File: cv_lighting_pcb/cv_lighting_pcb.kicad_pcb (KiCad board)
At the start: 2 copper layers, 81.3 x 73.7 mm, 27 parts, among them Q1 2N3906, U1 Current Driver, U2 Camera Input, U3 VO617A, U4 Barrel Jack

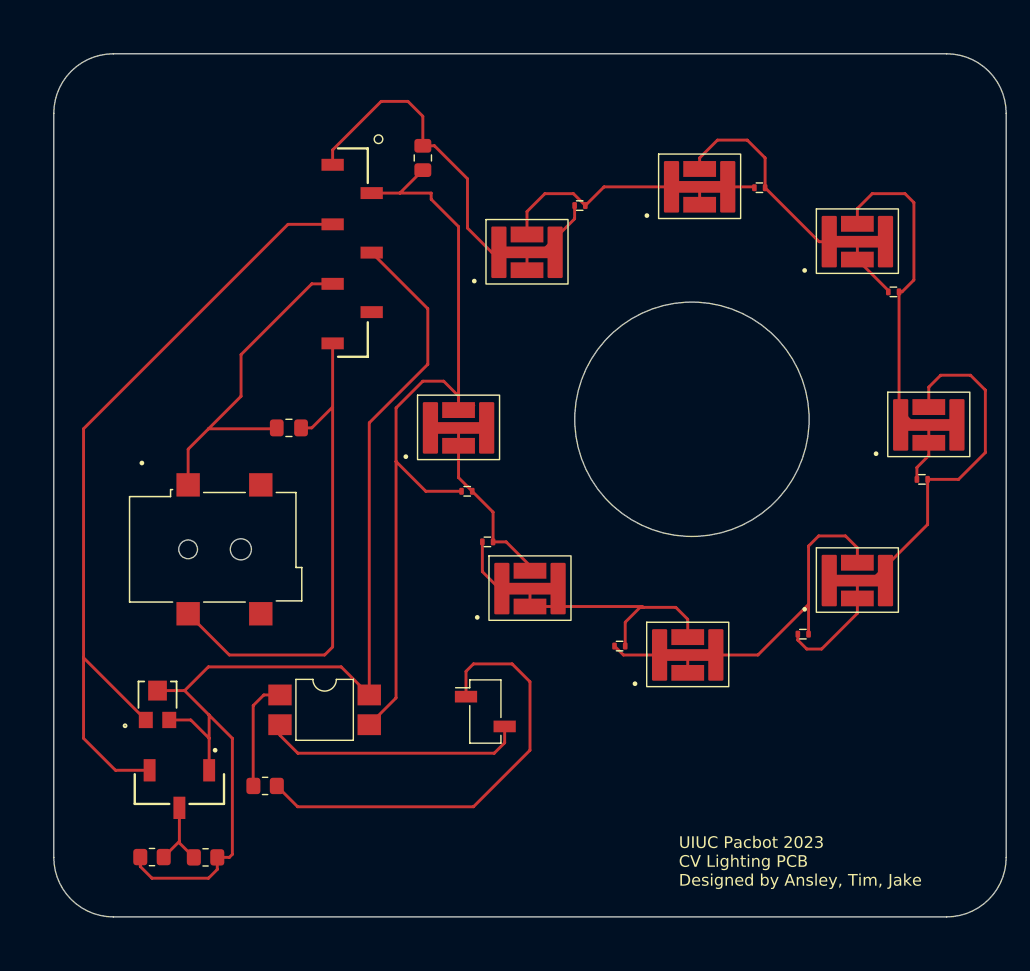
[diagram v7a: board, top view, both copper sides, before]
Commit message: more changes to lighting pcb
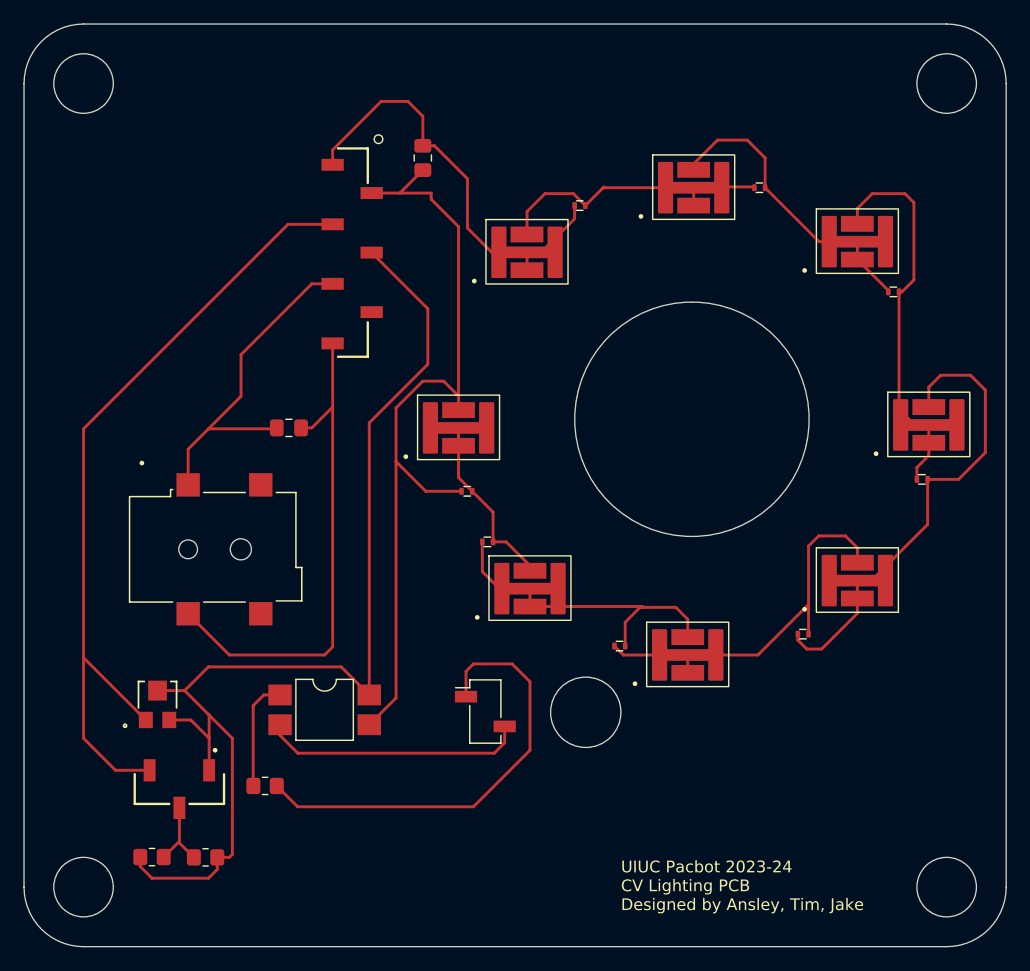
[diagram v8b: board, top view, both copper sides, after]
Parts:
- moved D2 0.51 mm to (156.2, 61.4)
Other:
- board size 81.3 x 73.7 mm -> 83.8 x 78.7 mm
- board text added: "UIUC Pacbot 2023-24 CV Lighting PCB Designed by Ansley, Tim, Jake"
- board text added: "hole for wire from camera to pcb"
- board text removed: "UIUC Pacbot 2023 CV Lighting PCB Designed by Ansley, Tim, Jake"
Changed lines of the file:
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@@
   )
   (footprint "cv_lighting_footprints:LED_SFH4715AS" (layer "F.Cu")
-    (at 156.718 61.359)
+    (at 156.21 61.4322)
     (property "Sheetfile" "cv_lighting_pcb.kicad_sch")
     (property "Sheetname" "")
@@
       (net 12 "Net-(Q1-C)") (pinfunction "C") (pintype "passive") (solder_mask_margin 0.102))
   )
-  (gr_arc (start 106.68 124.46) (mid 103.087898 122.972102) (end 101.6 119.38)
-    (stroke (width 0.1) (type default)) (layer "Edge.Cuts"))
+  (gr_circle (center 177.8 121.92) (end 180.34 121.92)
+    (stroke (width 0.1) (type default)) (fill none) (layer "Edge.Cuts"))
   (gr_circle (center 167.5892 81.9912) (end 167.5892 81.9912)
     (stroke (width 0.1) (type default)) (fill none) (layer "Edge.Cuts"))
-  (gr_line (start 182.88 55.88) (end 182.88 119.38)
+  (gr_line (start 182.88 53.34) (end 182.88 121.92)
     (stroke (width 0.1) (type default)) (layer "Edge.Cuts"))
-  (gr_line (start 106.68 50.8) (end 177.8 50.8)
+  (gr_circle (center 177.8 53.34) (end 180.34 53.34)
+    (stroke (width 0.1) (type default)) (fill none) (layer "Edge.Cuts"))
+  (gr_arc (start 182.88 121.92) (mid 181.392102 125.512102) (end 177.8 127)
     (stroke (width 0.1) (type default)) (layer "Edge.Cuts"))
-  (gr_arc (start 101.6 55.88) (mid 103.087898 52.287898) (end 106.68 50.8)
+  (gr_circle (center 104.14 121.92) (end 106.68 121.92)
+    (stroke (width 0.1) (type default)) (fill none) (layer "Edge.Cuts"))
+  (gr_arc (start 177.8 48.26) (mid 181.392102 49.747898) (end 182.88 53.34)
     (stroke (width 0.1) (type default)) (layer "Edge.Cuts"))
-  (gr_line (start 101.6 119.38) (end 101.6 55.88)
+  (gr_arc (start 104.14 127) (mid 100.547898 125.512102) (end 99.06 121.92)
     (stroke (width 0.1) (type default)) (layer "Edge.Cuts"))
-  (gr_line (start 177.8 124.46) (end 106.68 124.46)
+  (gr_line (start 104.14 48.26) (end 177.8 48.26)
+    (stroke (width 0.1) (type default)) (layer "Edge.Cuts"))
+  (gr_line (start 99.06 121.92) (end 99.06 53.34)
+    (stroke (width 0.1) (type default)) (layer "Edge.Cuts"))
+  (gr_circle (center 104.14 53.34) (end 106.68 53.34)
+    (stroke (width 0.1) (type default)) (fill none) (layer "Edge.Cuts"))
+  (gr_line (start 177.8 127) (end 104.14 127)
     (stroke (width 0.1) (type default)) (layer "Edge.Cuts"))
   (gr_circle (center 156.061042 81.9912) (end 166.061047 81.9912)
     (stroke (width 0.1) (type default)) (fill none) (layer "Edge.Cuts"))
-  (gr_arc (start 182.88 119.38) (mid 181.392102 122.972102) (end 177.8 124.46)
-    (stroke (width 0.1) (type default)) (layer "Edge.Cuts"))
-  (gr_arc (start 177.8 50.8) (mid 181.392102 52.287898) (end 182.88 55.88)
+  (gr_circle (center 147 107) (end 150 107)
+    (stroke (width 0.1) (type default)) (fill none) (layer "Edge.Cuts"))
+  (gr_arc (start 99.06 53.34) (mid 100.547898 49.747898) (end 104.14 48.26)
     (stroke (width 0.1) (type default)) (layer "Edge.Cuts"))
   (gr_circle (center 156.061042 81.9912) (end 176.381042 81.9912)
     (stroke (width 0.1) (type default)) (fill none) (layer "F.Fab"))
-  (gr_text "UIUC Pacbot 2023\nCV Lighting PCB\nDesigned by Ansley, Tim, Jake" (at 154.94 121.92) (layer "F.SilkS")
+  (gr_text "UIUC Pacbot 2023-24\nCV Lighting PCB\nDesigned by Ansley, Tim, Jake" (at 150 124) (layer "F.SilkS")
+    (effects (font (size 1 1) (thickness 0.15)) (justify left bottom))
+  )
+  (gr_text "hole for wire from camera to pcb\n\n" (at 146 113) (layer "F.Fab")
     (effects (font (size 1 1) (thickness 0.15)) (justify left bottom))
   )
@@
     (effects (font (size 1 1) (thickness 0.15)) (justify left bottom))
   )
-  (gr_text "Double check radius of circle based on camera" (at 140.414642 78.6384) (layer "F.Fab")
+  (gr_text "Double check radius of circle based on camera" (at 51 112) (layer "F.Fab")
     (effects (font (size 1 1) (thickness 0.15)) (justify left bottom))
   )
+  (segment (start 148.4862 62.2322) (end 156.21 62.2322) (width 0.25) (layer "F.Cu") (net 1))
   (segment (start 145.9484 62.738) (end 143.51 62.738) (width 0.25) (layer "F.Cu") (net 1))
   (segment (start 161.3206 62.159) (end 161.3916 62.23) (width 0.25) (layer "F.Cu") (net 1))
-  (segment (start 148.5594 62.159) (end 156.718 62.159) (width 0.25) (layer "F.Cu") (net 1))
   (segment (start 141.986 64.262) (end 141.986 66.2188) (width 0.25) (layer "F.Cu") (net 1))
   (segment (start 156.718 62.159) (end 161.3206 62.159) (width 0.25) (layer "F.Cu") (net 1))
   (segment (start 143.51 62.738) (end 141.986 64.262) (width 0.25) (layer "F.Cu") (net 1))
   (segment (start 146.9644 63.754) (end 145.9484 62.738) (width 0.25) (layer "F.Cu") (net 1))
-  (segment (start 156.718 62.159) (end 156.718 63.6808) (width 0.25) (layer "F.Cu") (net 1))
-  (segment (start 146.9644 63.754) (end 148.5594 62.159) (width 0.25) (layer "F.Cu") (net 1))
+  (segment (start 148.4122 62.3062) (end 148.4862 62.2322) (width 0.25) (layer "F.Cu") (net 1))
+  (segment (start 156.21 62.2322) (end 156.21 63.754) (width 0.25) (layer "F.Cu") (net 1))
+  (segment (start 146.9644 63.754) (end 148.4122 62.3062) (width 0.25) (layer "F.Cu") (net 1))
+  (segment (start 148.4122 62.3062) (end 148.5594 62.159) (width 0.25) (layer "F.Cu") (net 1))
   (segment (start 141.986 67.747) (end 141.986 69.2688) (width 0.25) (layer "F.Cu") (net 2))
   (segment (start 146.05 64.883) (end 143.186 67.747) (width 0.25) (layer "F.Cu") (net 2))
@@
   (segment (start 129.54 54.864) (end 131.826 54.864) (width 0.25) (layer "F.Cu") (net 2))
   (segment (start 131.826 54.864) (end 133.096 56.134) (width 0.25) (layer "F.Cu") (net 2))
-  (segment (start 156.718 59.69) (end 158.242 58.166) (width 0.25) (layer "F.Cu") (net 3))
-  (segment (start 156.718 60.6308) (end 156.718 59.69) (width 0.25) (layer "F.Cu") (net 3))
   (segment (start 160.782 58.166) (end 162.306 59.69) (width 0.25) (layer "F.Cu") (net 3))
+  (segment (start 158.242 58.166) (end 156.21 60.198) (width 0.25) (layer "F.Cu") (net 3))
   (segment (start 170.18 66.84) (end 166.916 66.84) (width 0.25) (layer "F.Cu") (net 3))
+  (segment (start 156.21 60.198) (end 156.21 60.704) (width 0.25) (layer "F.Cu") (net 3))
   (segment (start 170.18 67.165) (end 171.9146 67.165) (width 0.25) (layer "F.Cu") (net 3))
   (segment (start 170.18 66.84) (end 170.18 68.3618) (width 0.25) (layer "F.Cu") (net 3))
